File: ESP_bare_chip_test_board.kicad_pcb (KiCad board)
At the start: 4 copper layers, 57.1 x 63.5 mm, 91 parts, among them J1101 Conn_01x04, J1201 NorComp - 112-024-113RYY1, J1301 Conn_01x06, J1302 Conn_01x06, J1501 Conn_01x04, J1502 Conn_01x04, J201 Conn_01x06, J501 Barrel_Jack, J502 PWR_IN, J503 ALTERNATE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

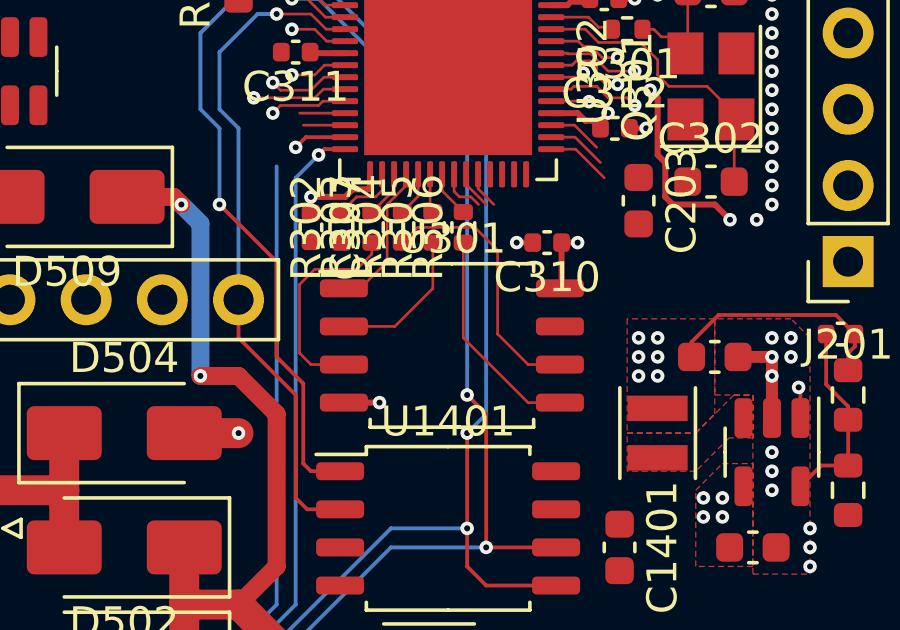
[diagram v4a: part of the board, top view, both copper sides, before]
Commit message: Fixup ESP flash memory wiring
One of the wires was missing, so added it. Rearranged wiring to allow it
to fit without having to via across layers.
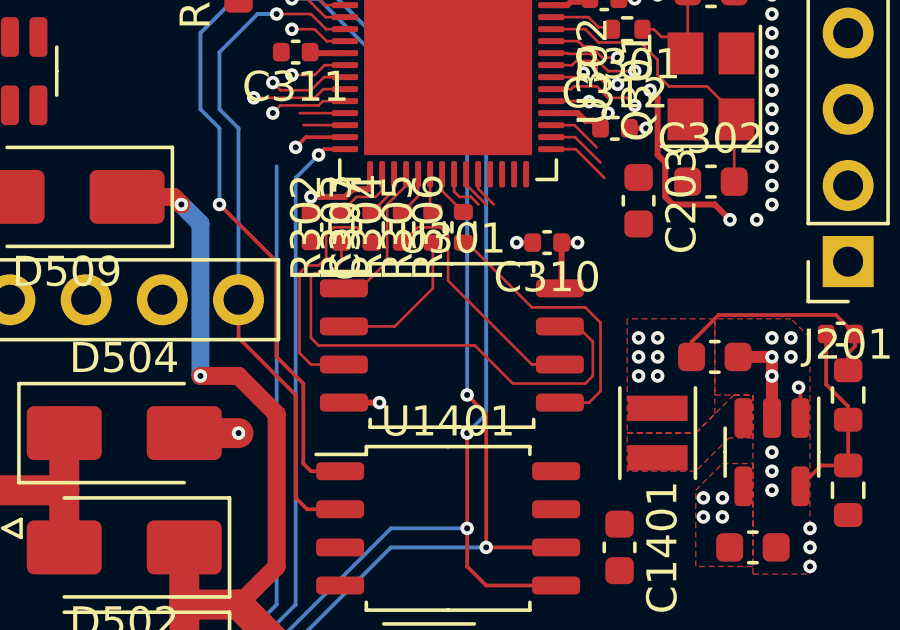
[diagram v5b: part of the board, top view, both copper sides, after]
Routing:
- net /ESP32-S3/ESP32-S3-core/SPIHD: track 0.00 -> 16.5 mm
- net /ESP32-S3/ESP32-S3-core/SPID: track 7.29 -> 9.47 mm
- net /ESP32-S3/ESP32-S3-core/SPIWP: track 7.14 -> 8.01 mm
- net /ESP32-S3/ESP32-S3-core/SPICLK: track 8.99 -> 8.25 mm

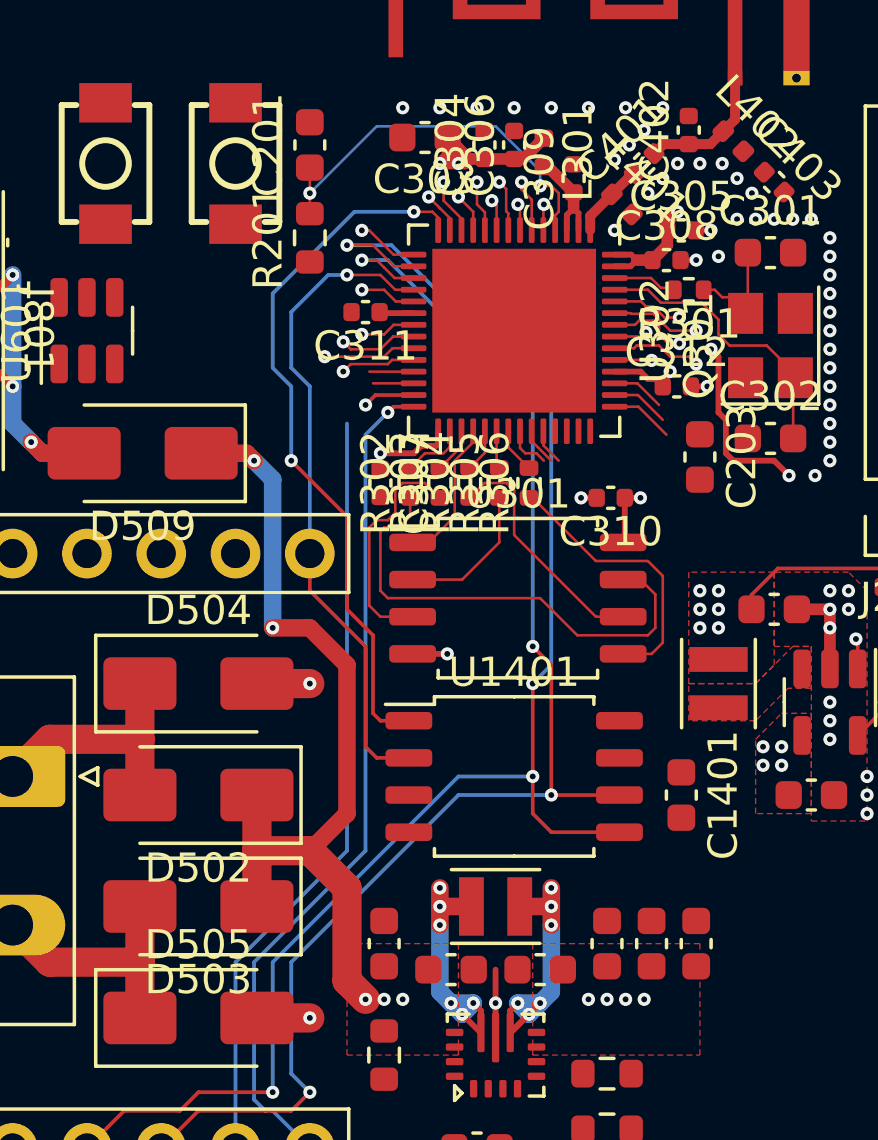
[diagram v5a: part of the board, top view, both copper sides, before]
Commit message: More wiring - Ethernet, SPI flash
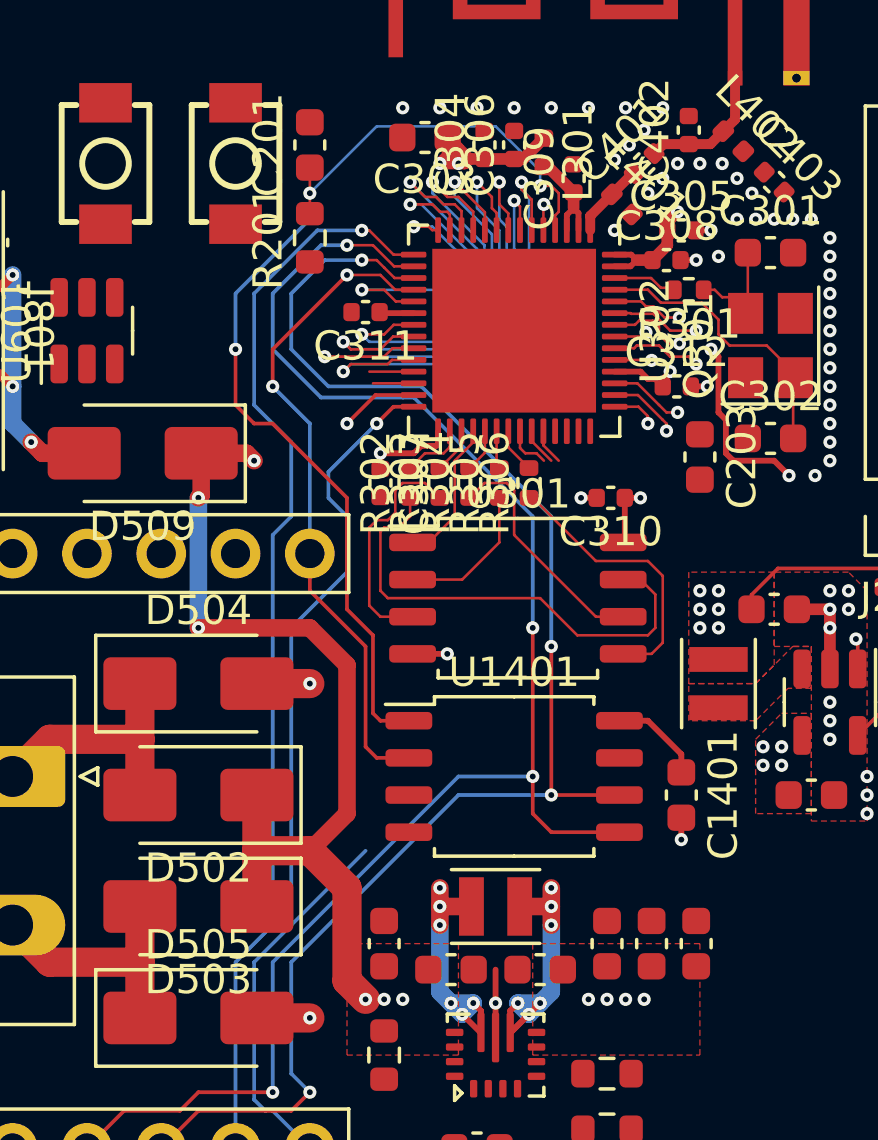
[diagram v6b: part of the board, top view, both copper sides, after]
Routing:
- net /~{ETH_CS0}: track 28.5 -> 37.2 mm
- net /ESP32-S3/IO14: track 1.93 -> 9.08 mm
- net /ESP32-S3/IO17: track 3.16 -> 10.2 mm
- net /ESP32-S3/IO18: track 2.57 -> 9.14 mm
- net /ESP32-S3/IO16: track 2.69 -> 9.15 mm
- net /ESP32-S3/IO7: track 1.90 -> 8.12 mm
- net /ESP32-S3/IO6: track 1.34 -> 7.41 mm
- net /ESP32-S3/IO15: track 1.90 -> 7.86 mm
- net /ESP32-S3/IO8: track 1.43 -> 6.83 mm
- net /ESP32-S3/IO4: track 1.07 -> 6.21 mm
- net /ESP32-S3/IO5: track 1.75 -> 6.70 mm
- net /ESP32-S3/IO1: track 1.79 -> 6.28 mm
- net /ESP32-S3/IO3: track 1.77 -> 6.26 mm
- net /~{ETH_INT}: track 28.9 -> 33.1 mm
- net /CLK: track 47.7 -> 51.8 mm
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
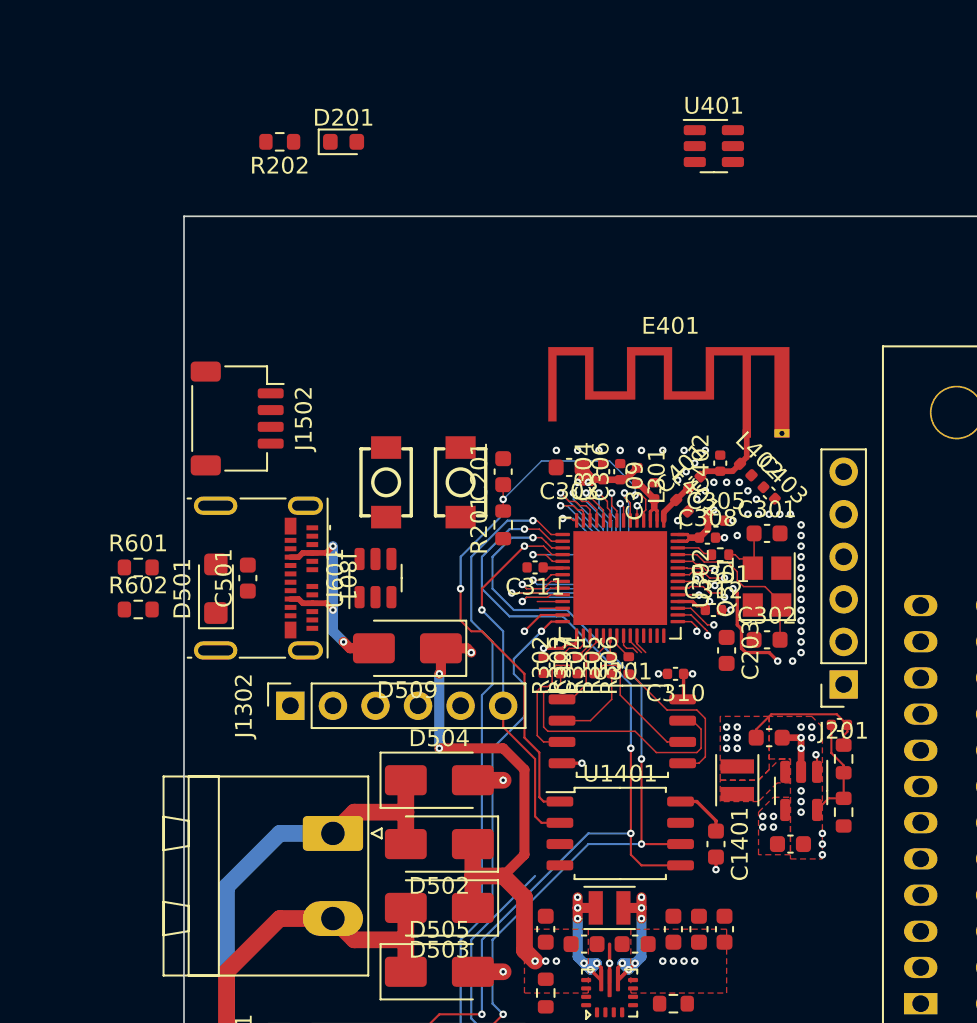
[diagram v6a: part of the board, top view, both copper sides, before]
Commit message: More wiring - GPIB connector, partially routed
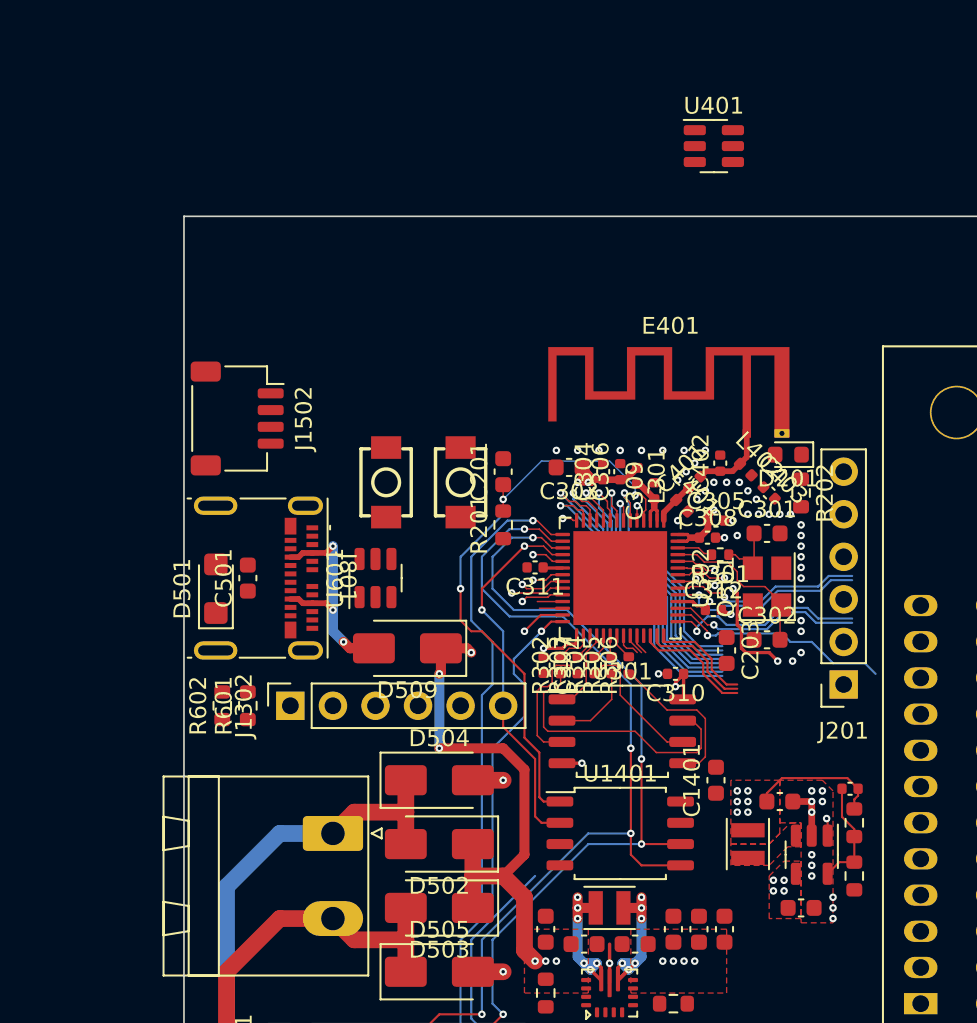
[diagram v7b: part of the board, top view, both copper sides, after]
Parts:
- moved R202 37.5 mm to (151.1, 63.5), turned to -90 degrees
- moved D201 32.5 mm to (150.4, 61.2), turned to 180 degrees
- moved R601 10.5 mm to (118.1, 76.2), turned to 90 degrees
- moved R602 7.63 mm to (116.6, 76.2), turned to 90 degrees
- moved C1003 3.86 mm to (149.9, 81.9)
- moved L1001 3.86 mm to (148.0, 84.5)
- moved R1001 3.86 mm to (154.3, 83.2)
- moved R1002 3.86 mm to (154.3, 86.4)
- moved C1001 3.86 mm to (151.1, 88.3)
- moved C1002 3.86 mm to (154.1, 81.2)
- moved U1001 3.86 mm to (151.8, 85.1)
- moved C1401 3.81 mm to (146.1, 80.6), turned to 90 degrees
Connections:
- J1201 pad 13: /ESP32-S3/IO17 -> /ESP32-S3/IO38
- J1201 pad 14: /ESP32-S3/IO16 -> /ESP32-S3/IO37
- J1201 pad 15: /ESP32-S3/IO15 -> /ESP32-S3/IO36
- J1201 pad 16: /ESP32-S3/IO14 -> /ESP32-S3/IO35
- J1201 pad 3: /ESP32-S3/IO21 -> /ESP32-S3/IO40
- J1201 pad 4: /ESP32-S3/IO18 -> /ESP32-S3/IO39
- J1502 pad 3: /ESP32-S3/IO35 -> /piicodev_connectors/J1_pin3
- J1502 pad 4: /ESP32-S3/IO36 -> /piicodev_connectors/J1_pin4
- U1501 pad 4: /ESP32-S3/IO35 -> /piicodev_connectors/J1_pin3
- U1501 pad 6: /ESP32-S3/IO36 -> /piicodev_connectors/J1_pin4
- U302 pad 42: /4pin_connector/J0_pin3 -> /ESP32-S3/IO37
- U302 pad 43: /4pin_connector/J0_pin4 -> /ESP32-S3/IO38
- U302 pad 44: /ESP32-S3/IO35 -> /ESP32-S3/IO39
- U302 pad 45: /ESP32-S3/IO36 -> /ESP32-S3/IO40
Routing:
- net /ESP32-S3/IO39: track 0.00 -> 13.5 mm, vias 0 -> 1
- net /ESP32-S3/IO38: track 0.00 -> 12.2 mm, vias 0 -> 1
- net /ESP32-S3/IO40: track 0.00 -> 11.6 mm, vias 0 -> 1
- net /ESP32-S3/IO8: track 6.83 -> 17.8 mm
- net /ESP32-S3/IO7: track 8.12 -> 18.7 mm
- net /ESP32-S3/IO41: track 1.27 -> 11.8 mm
- net /ESP32-S3/IO6: track 7.41 -> 17.7 mm
- net /ESP32-S3/IO5: track 6.70 -> 16.7 mm
- net /ESP32-S3/IO4: track 6.21 -> 15.9 mm
- net /ESP32-S3/IO3: track 6.26 -> 15.1 mm
- net /ESP32-S3/IO2: track 4.54 -> 13.3 mm
- net /ESP32-S3/IO42: track 3.09 -> 11.4 mm
- net /ESP32-S3/IO1: track 6.28 -> 14.2 mm
- net /ESP32-S3/IO14: track 9.08 -> 1.93 mm
- net /ESP32-S3/IO17: track 10.2 -> 3.16 mm
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
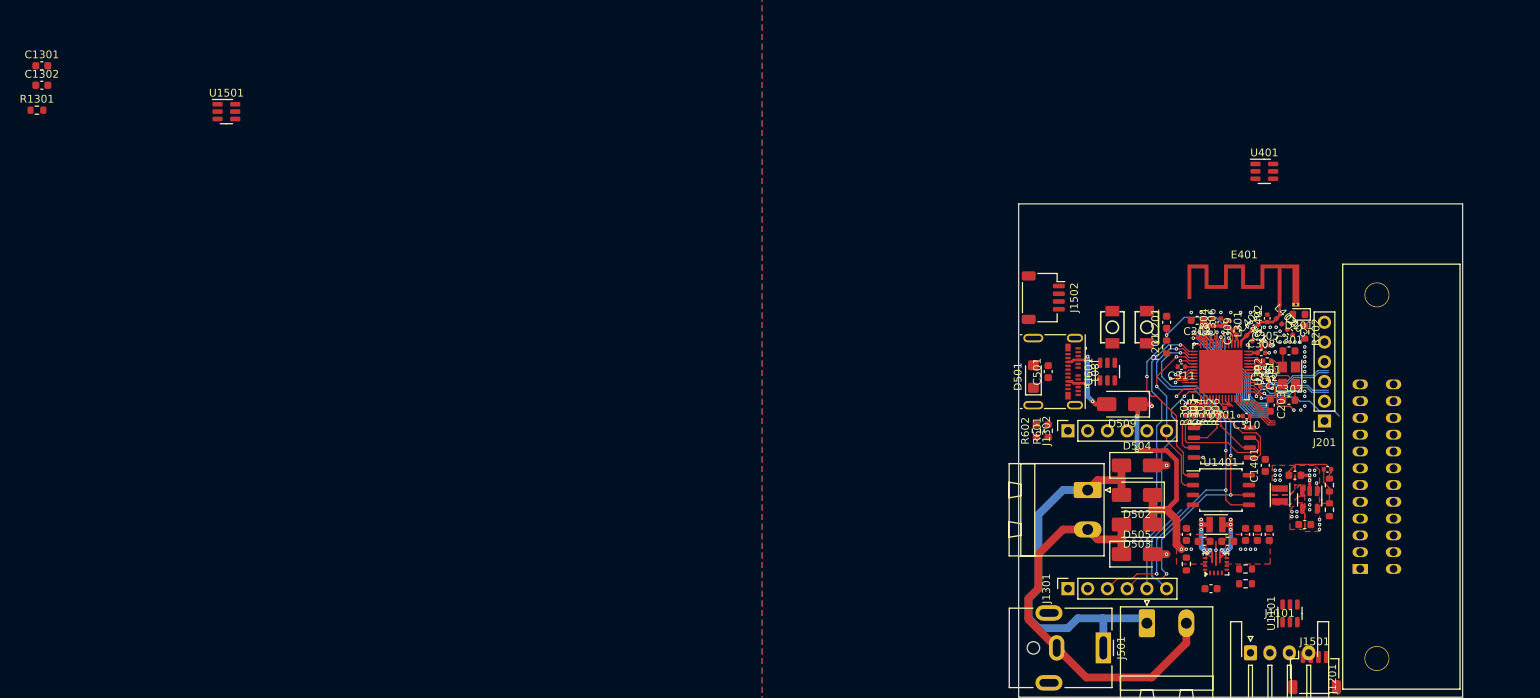
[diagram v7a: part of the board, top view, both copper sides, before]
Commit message: partial! Ran wires for GPIB connector
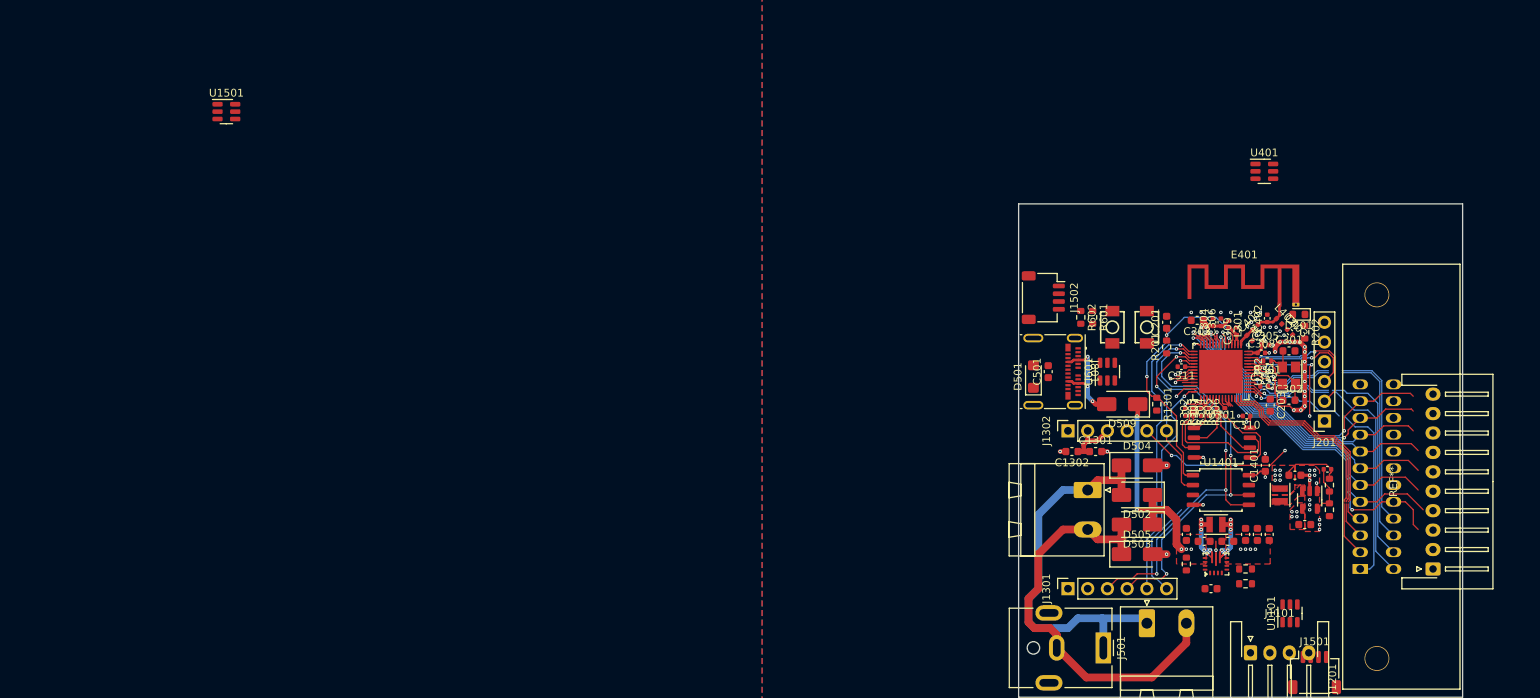
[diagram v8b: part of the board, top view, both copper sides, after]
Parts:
- added REF**: JST_XH_S10B-XH-A-1_1x10_P2.50mm_Horizontal, Connector_JST:JST_XH_S10B-XH-A-1_1x10_P2.50mm_Horizontal, F.Cu at (167.6, 94.0)
- moved R1301 149.0 mm to (132.1, 72.8), turned to -90 degrees
- moved C1301 144.4 mm to (124.2, 78.9)
- moved C1302 140.7 mm to (121.2, 78.9), turned to 180 degrees
- moved R601 15.7 mm to (123.8, 61.6), turned to -90 degrees
- moved R602 15.7 mm to (122.3, 61.6), turned to -90 degrees
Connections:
- J1201 pad 10: /ESP32-S3/IO3 -> /ESP32-S3/IO2
- J1201 pad 11: /ESP32-S3/IO2 -> /ESP32-S3/IO1
- J1201 pad 17: /ESP32-S3/IO1 -> /ESP32-S3/IO8
- J1201 pad 5: /ESP32-S3/IO8 -> /ESP32-S3/IO7
- J1201 pad 6: /ESP32-S3/IO7 -> /ESP32-S3/IO6
- J1201 pad 7: /ESP32-S3/IO6 -> /ESP32-S3/IO5
- J1201 pad 8: /ESP32-S3/IO5 -> /ESP32-S3/IO4
- J1201 pad 9: /ESP32-S3/IO4 -> /ESP32-S3/IO3
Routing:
- net /ESP32-S3/IO37: track 6.14 -> 50.6 mm
- net /ESP32-S3/IO36: track 6.71 -> 50.0 mm
- net /ESP32-S3/IO35: track 7.20 -> 48.2 mm
- net /ETH_RST: track 2.44 -> 41.5 mm, vias 1 -> 6
- net /ESP32-S3/IO8: track 17.8 -> 48.3 mm, vias 1 -> 2
- net /ESP32-S3/IO7: track 18.7 -> 46.9 mm
- net /ESP32-S3/IO38: track 12.2 -> 39.5 mm
- net /ESP32-S3/IO6: track 17.7 -> 43.2 mm
- net /ESP32-S3/IO1: track 14.2 -> 38.0 mm, vias 1 -> 2
- net /ESP32-S3/IO42: track 11.4 -> 35.1 mm
- net /ESP32-S3/IO5: track 16.7 -> 40.2 mm
- net /ESP32-S3/IO4: track 15.9 -> 38.3 mm
- net /ESP32-S3/IO2: track 13.3 -> 35.6 mm, vias 1 -> 2
- net /ESP32-S3/IO3: track 15.1 -> 36.7 mm
- net /ESP32-S3/UART0_Tx: track 1.13 -> 19.9 mm, vias 1 -> 2
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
